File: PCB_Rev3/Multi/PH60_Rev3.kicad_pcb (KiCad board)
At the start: 2 copper layers, 285 x 94.6 mm, 213 parts, among them J1 Conn_01x02_Pin, J2 Conn_01x02_Pin, J3 USB_C_Receptacle_USB2.0_16P, J4 Conn_01x04_Socket, U1 TP4057, U2 nRF52840, U4 TPS2116DRL, X1 32.768kHz, X2 Crystal_Generic

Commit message: mcu走线间距线宽调整至0.15mm，vbus与vddout滤波电容布局调整
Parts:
- moved C20 0.95 mm to (63.7, 71.4), turned to 0 degrees
- moved C19 0.56 mm to (55.1, 74.8), turned to -90 degrees
- moved C2 0.52 mm to (49.8, 70.2)
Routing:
- net GND: track 21.8 -> 23.4 mm, vias 96 -> 113
- net /DEC4: track 14.8 -> 13.4 mm
- net col_3: track 127.5 -> 126.8 mm
- net Net-(U2-XL2/P0.01): track 4.85 -> 5.60 mm
- net col_4: track 179.3 -> 178.7 mm

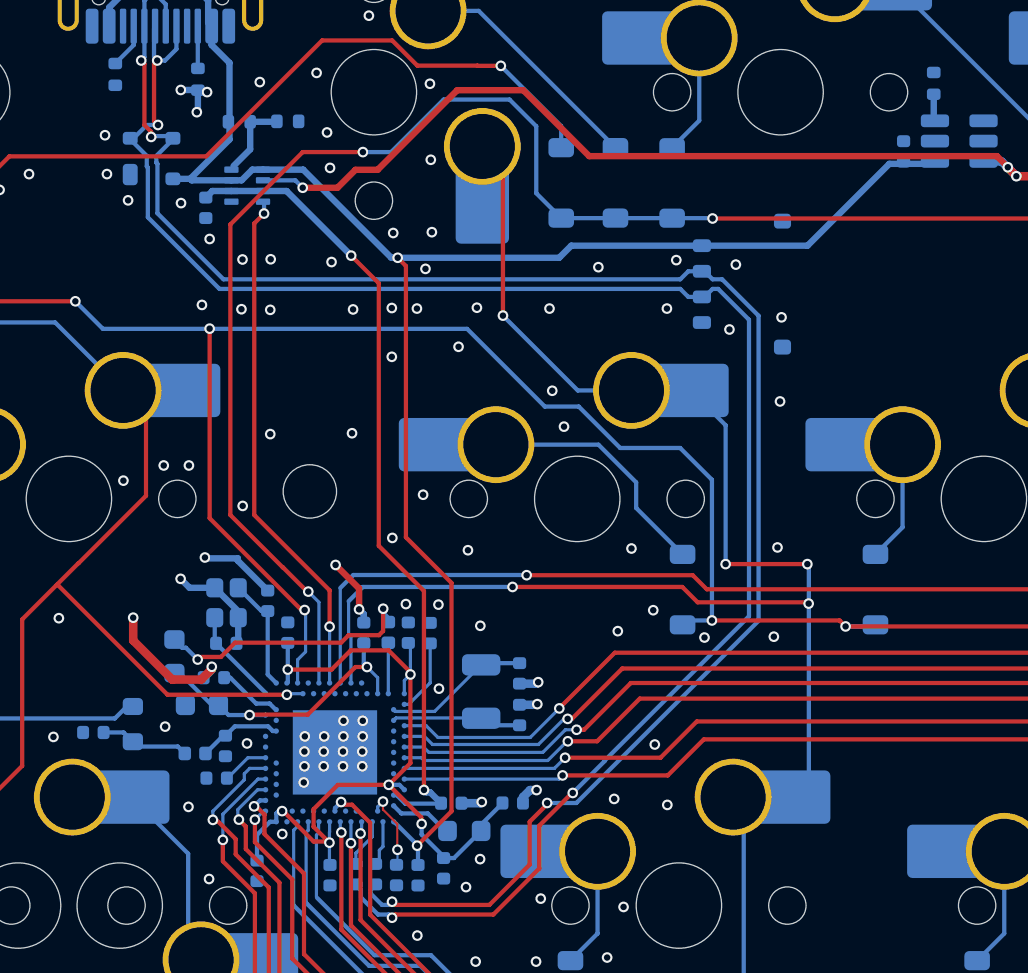
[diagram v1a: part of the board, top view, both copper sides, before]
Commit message: 放置部分gnd过孔
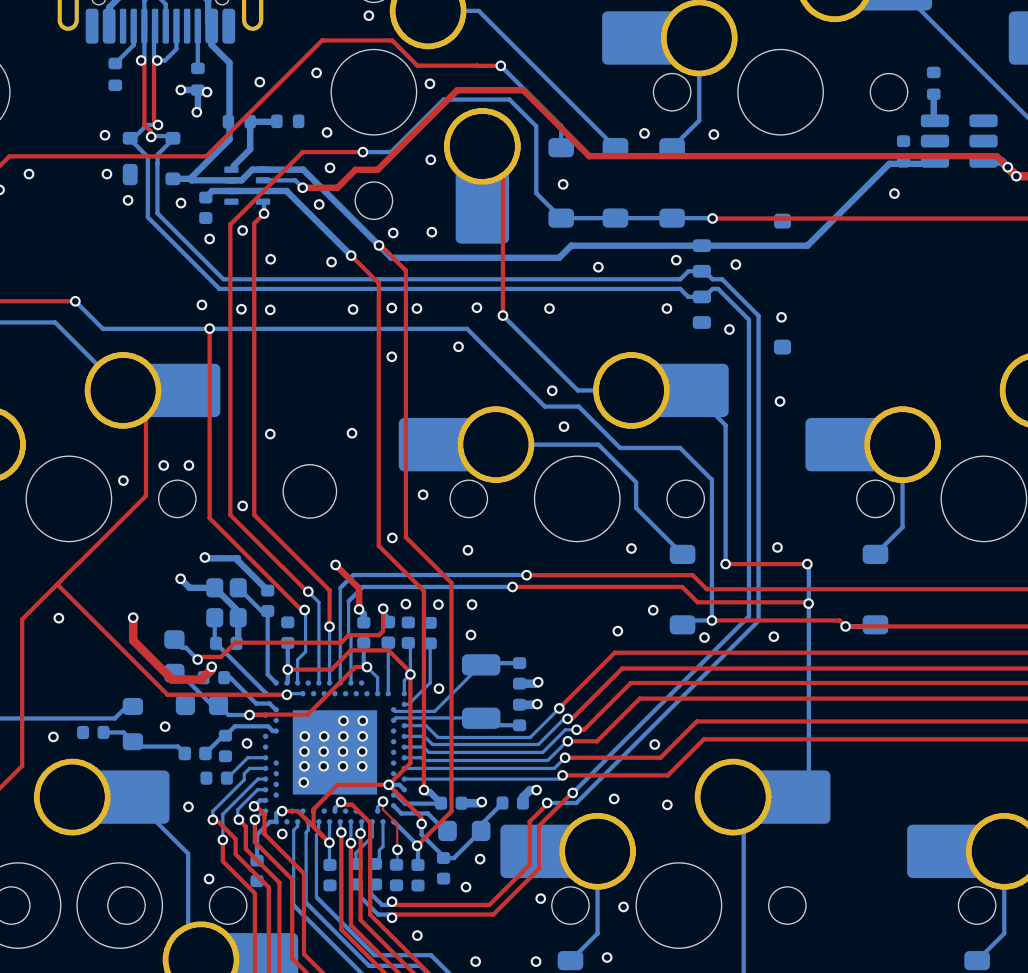
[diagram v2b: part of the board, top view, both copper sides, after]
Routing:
- net VBUS: track 86.9 -> 87.9 mm
- net GND: vias 113 -> 118

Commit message: DRC check
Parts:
- moved J4 21.2 mm to (95.5, 48.1)
- moved D17 2.20 mm to (69.4, 61.4)
- moved C8 1.75 mm to (63.7, 63.6)
- moved C10 1.65 mm to (63.7, 65.6)
- moved X1 1.54 mm to (61.9, 64.7)
- moved J1 1.41 mm to (146.1, 104.5)
- moved J2 1.16 mm to (148.3, 113.0)
- moved R2 0.74 mm to (52.6, 40.0), turned to -90 degrees
- moved D1 0.14 mm to (46.7, 41.1), turned to 180 degrees
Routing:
- net +BATT: track 115.3 -> 44.3 mm, vias 5 -> 0
- net row_0: track 287.3 -> 308.7 mm, vias 14 -> 6
- net Net-(D64-A): track 11.9 -> 28.5 mm
- net col_12: track 340.1 -> 353.3 mm
- net Net-(D65-A): track 19.3 -> 31.8 mm
- net col_11: track 303.3 -> 315.7 mm
- net col_13: track 352.7 -> 364.8 mm
- net Net-(D66-A): track 19.2 -> 31.0 mm
- net VBUS: track 87.9 -> 99.1 mm, vias 2 -> 3
- net col_10: track 277.2 -> 287.9 mm
- net col_4: track 178.7 -> 182.0 mm
- net col_3: track 126.8 -> 129.4 mm
- net /USB_D-: track 83.7 -> 81.7 mm, vias 4 -> 2
- net col_2: track 136.6 -> 138.3 mm
- net /SWCLK: track 116.4 -> 114.9 mm
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- added copper zone on B.Cu, net +BATT
